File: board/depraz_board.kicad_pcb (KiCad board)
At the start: 2 copper layers, 60 x 40 mm, 43 parts, among them J1 Switches, J2 Host, J3 SWD, J4 SERIAL, U1 TLV75519PDRV, U2 TLV75533PDRV, U5 PMW3389DM, U6 STM32F103C8Tx, Y1 8MHz

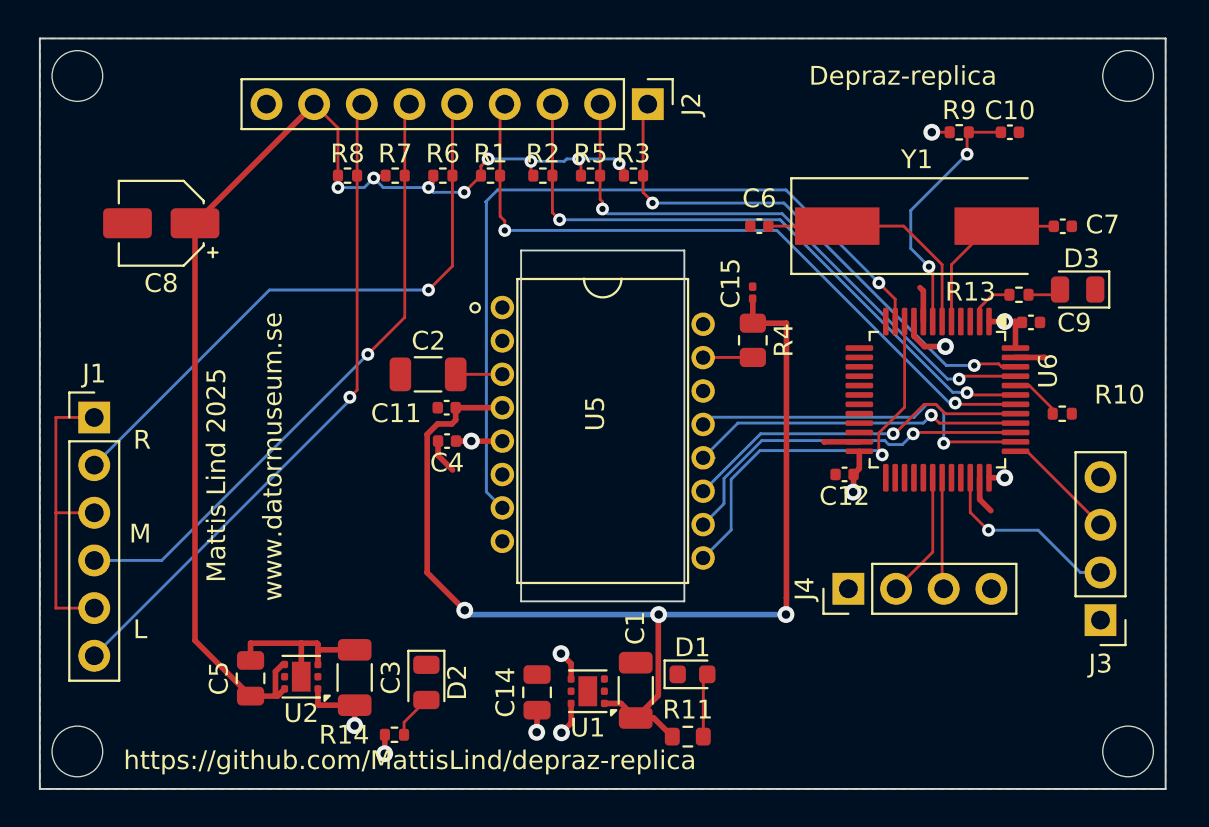
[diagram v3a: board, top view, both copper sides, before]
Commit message: Fixed layout after review.
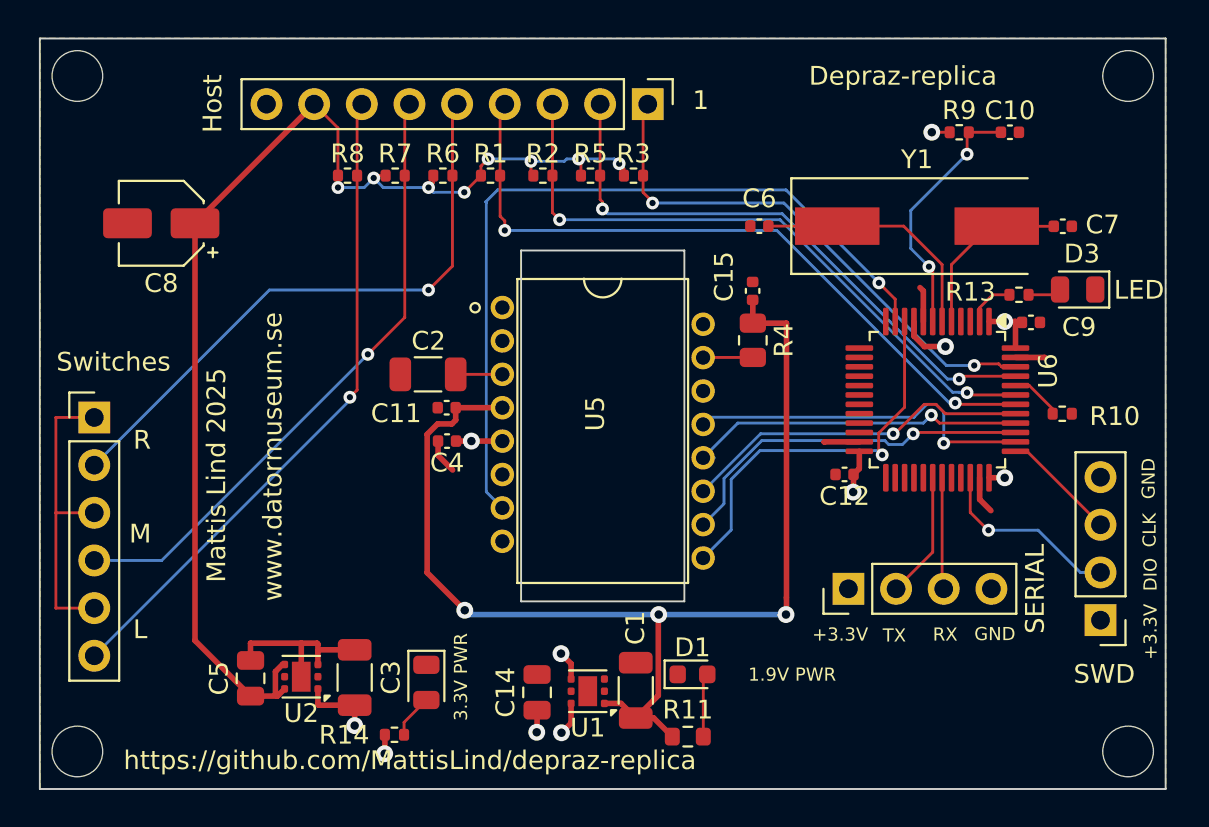
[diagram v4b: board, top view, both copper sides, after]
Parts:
- C15: footprint Capacitor_SMD:C_0201_0603Metric -> Capacitor_SMD:C_0402_1005Metric
- moved C15 0.09 mm to (158.0, 73.5)
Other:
- board text added: "+3.3V"
- board text added: "1"
- board text added: "CLK"
- board text added: "DIO"
- board text added: "GND"
- board text added: "RX"
- board text added: "TX"
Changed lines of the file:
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@@
 			(at 0 -2.33 0)
 			(layer "F.SilkS")
+			(hide yes)
 			(effects
 				(font
@@
 		)
 		(property "Value" "Switches"
-			(at 0 15.03 0)
-			(layer "F.Fab")
+			(at 1.0266 -2.9586 0)
+			(layer "F.SilkS")
 			(effects
 				(font
@@
 			(at 0 -2.33 0)
 			(layer "F.SilkS")
+			(hide yes)
 			(effects
 				(font
@@
 		)
 		(property "Value" "SWD"
-			(at 0 9.95 0)
-			(layer "F.Fab")
+			(at -0.2032 -2.8784 0)
+			(layer "F.SilkS")
 			(effects
 				(font
@@
 			(at 0 -2.33 90)
 			(layer "F.SilkS")
+			(hide yes)
 			(effects
 				(font
@@
 		)
 		(property "Value" "Host"
-			(at 0 22.65 90)
-			(layer "F.Fab")
+			(at -0.0254 23.1902 90)
+			(layer "F.SilkS")
 			(effects
 				(font
@@
 			(at 0 -2.33 90)
 			(layer "F.SilkS")
+			(hide yes)
 			(effects
 				(font
@@
 		(property "Value" "SERIAL"
 			(at 0 9.95 90)
-			(layer "F.Fab")
+			(layer "F.SilkS")
 			(effects
 				(font
@@
 		(tags "resistor")
 		(property "Reference" "R10"
-			(at 3.056 -1.006 0)
+			(at 2.802 0.137 0)
 			(layer "F.SilkS")
 			(effects
@@
 		(tags "LED")
 		(property "Reference" "D3"
-			(at -0.2032 1.651 360)
+			(at -0.2286 1.905 360)
 			(layer "F.SilkS")
 			(effects
@@
 		)
 		(property "Value" "LED"
-			(at 0 1.65 360)
-			(layer "F.Fab")
+			(at -3.2766 -0.0254 0)
+			(layer "F.SilkS")
 			(effects
 				(font
@@
 		)
 		(property "Value" "1.9V PWR"
-			(at 0 1.43 0)
-			(layer "F.Fab")
+			(at 5.3137 0.0138 0)
+			(layer "F.SilkS")
 			(effects
 				(font
-					(size 1 1)
-					(thickness 0.15)
+					(size 0.7 0.7)
+					(thickness 0.1)
 				)
 			)
@@
 		(tags "LED")
 		(property "Reference" "D2"
-			(at 0 -1.65 90)
+			(at 2.4794 -0.1668 90)
 			(layer "F.SilkS")
+			(hide yes)
 			(effects
 				(font
@@
 		)
 		(property "Value" "3.3V PWR"
-			(at 0 1.65 90)
-			(layer "F.Fab")
+			(at -0.2892 -1.8432 90)
+			(layer "F.SilkS")
 			(effects
 				(font
-					(size 1 1)
-					(thickness 0.15)
+					(size 0.7 0.7)
+					(thickness 0.1)
 				)
 			)
@@
 		)
 	)
-	(footprint "Capacitor_SMD:C_0201_0603Metric"
+	(footprint "Capacitor_SMD:C_0402_1005Metric"
 		(layer "F.Cu")
-		(at 157.988 73.5482 90)
-		(descr "Capacitor SMD 0201 (0603 Metric), square (rectangular) end terminal, IPC_7351 nominal, (Body size source: https://www.vishay.com/docs/20052/crcw0201e3.pdf), generated with kicad-footprint-generator")
+		(at 157.988 73.4542 90)
+		(descr "Capacitor SMD 0402 (1005 Metric), square (rectangular) end terminal, IPC_7351 nominal, (Body size source: IPC-SM-782 page 76, https://www.pcb-3d.com/wordpress/wp-content/uploads/ipc-sm-782a_amendment_1_and_2.pdf), generated with kicad-footprint-generator")
 		(tags "capacitor")
 		(property "Reference" "C15"
-			(at 0.4978 -1.1684 90)
+			(at 0.7594 -1.524 90)
 			(layer "F.SilkS")
 			(effects
@@
 		)
 		(property "Value" "100n"
-			(at 0 1.05 90)
+			(at 0 1.16 90)
 			(layer "F.Fab")
 			(effects
@@
 			)
 		)
-		(property "Footprint" "Capacitor_SMD:C_0201_0603Metric"
+		(property "Footprint" "Capacitor_SMD:C_0402_1005Metric"
 			(at 0 0 90)
 			(unlocked yes)
@@
 		(attr smd)
 		(fp_line
-			(start 0.7 -0.35)
-			(end 0.7 0.35)
+			(start -0.107836 -0.36)
+			(end 0.107836 -0.36)
+			(stroke
+				(width 0.12)
+				(type solid)
+			)
+			(layer "F.SilkS")
+		)
+		(fp_line
+			(start -0.107836 0.36)
+			(end 0.107836 0.36)
+			(stroke
+				(width 0.12)
+				(type solid)
+			)
+			(layer "F.SilkS")
+		)
+		(fp_line
+			(start 0.91 -0.46)
+			(end 0.91 0.46)
 			(stroke
 				(width 0.05)
@@
 		)
 		(fp_line
-			(start -0.7 -0.35)
-			(end 0.7 -0.35)
+			(start -0.91 -0.46)
+			(end 0.91 -0.46)
 			(stroke
 				(width 0.05)
@@
 		)
 		(fp_line
-			(start 0.7 0.35)
-			(end -0.7 0.35)
+			(start 0.91 0.46)
+			(end -0.91 0.46)
 			(stroke
 				(width 0.05)
@@
 		)
 		(fp_line
-			(start -0.7 0.35)
-			(end -0.7 -0.35)
+			(start -0.91 0.46)
+			(end -0.91 -0.46)
 			(stroke
 				(width 0.05)
@@
 		)
 		(fp_line
-			(start 0.3 -0.15)
-			(end 0.3 0.15)
+			(start 0.5 -0.25)
+			(end 0.5 0.25)
 			(stroke
 				(width 0.1)
@@
 		)
 		(fp_line
-			(start -0.3 -0.15)
-			(end 0.3 -0.15)
+			(start -0.5 -0.25)
+			(end 0.5 -0.25)
 			(stroke
 				(width 0.1)
@@
 		)
 		(fp_line
-			(start 0.3 0.15)
-			(end -0.3 0.15)
+			(start 0.5 0.25)
+			(end -0.5 0.25)
 			(stroke
 				(width 0.1)
@@
 		)
 		(fp_line
-			(start -0.3 0.15)
-			(end -0.3 -0.15)
+			(start -0.5 0.25)
+			(end -0.5 -0.25)
 			(stroke
 				(width 0.1)
@@
 		)
 		(fp_text user "${REFERENCE}"
-			(at 0 -0.68 90)
+			(at 0 0 90)
 			(layer "F.Fab")
 			(effects
@@
 			)
 		)
-		(pad "" smd roundrect
-			(at -0.345 0 90)
-			(size 0.318 0.36)
-			(layers "F.Paste")
-			(roundrect_rratio 0.25)
-		)
-		(pad "" smd roundrect
-			(at 0.345 0 90)
-			(size 0.318 0.36)
-			(layers "F.Paste")
-			(roundrect_rratio 0.25)
-		)
 		(pad "1" smd roundrect
-			(at -0.32 0 90)
-			(size 0.46 0.4)
-			(layers "F.Cu" "F.Mask")
+			(at -0.48 0 90)
+			(size 0.56 0.62)
+			(layers "F.Cu" "F.Paste" "F.Mask")
 			(roundrect_rratio 0.25)
 			(net 53 "+1.9V")
@@
 		)
 		(pad "2" smd roundrect
-			(at 0.32 0 90)
-			(size 0.46 0.4)
-			(layers "F.Cu" "F.Mask")
+			(at 0.48 0 90)
+			(size 0.56 0.62)
+			(layers "F.Cu" "F.Paste" "F.Mask")
 			(roundrect_rratio 0.25)
 			(net 1 "GND")
 			(pintype "passive")
 		)
-		(model "${KICAD8_3DMODEL_DIR}/Capacitor_SMD.3dshapes/C_0201_0603Metric.wrl"
+		(model "${KICAD8_3DMODEL_DIR}/Capacitor_SMD.3dshapes/C_0402_1005Metric.wrl"
 			(offset
 				(xyz 0 0 0)
@@
 		(tags "capacitor")
 		(property "Reference" "C9"
-			(at 2.3088 0.0254 0)
+			(at 2.5628 0.254 0)
 			(layer "F.SilkS")
 			(effects
@@
 		(layer "Edge.Cuts")
 	)
+	(gr_text "CLK"
+		(at 179.5526 87.122 90)
+		(layer "F.SilkS")
+		(effects
+			(font
+				(size 0.7 0.7)
+				(thickness 0.1)
+			)
+			(justify left bottom)
+		)
+	)
 	(gr_text "M"
 		(at 125.35 86.4 0)
@@
 		)
 	)
+	(gr_text "RX"
+		(at 167.5892 92.1766 0)
+		(layer "F.SilkS")
+		(effects
+			(font
+				(size 0.7 0.7)
+				(thickness 0.1)
+			)
+			(justify left bottom)
+		)
+	)
 	(gr_text "R"
 		(at 125.45 81.4 0)
@@
 		)
 	)
+	(gr_text "GND"
+		(at 179.5018 84.5566 90)
+		(layer "F.SilkS")
+		(effects
+			(font
+				(size 0.7 0.7)
+				(thickness 0.1)
+			)
+			(justify left bottom)
+		)
+	)
+	(gr_text "+3.3V"
+		(at 161.163 92.1766 0)
+		(layer "F.SilkS")
+		(effects
+			(font
+				(size 0.7 0.7)
+				(thickness 0.1)
+			)
+			(justify left bottom)
+		)
+	)
 	(gr_text "Depraz-replica"
 		(at 166 62 0)
@@
 		)
 	)
+	(gr_text "DIO"
+		(at 179.6034 89.4588 90)
+		(layer "F.SilkS")
+		(effects
+			(font
+				(size 0.7 0.7)
+				(thickness 0.1)
+			)
+			(justify left bottom)
+		)
+	)
 	(gr_text "www.datormuseum.se"
 		(at 133 90 90)
@@
 		)
 	)
+	(gr_text "TX"
+		(at 164.9222 92.2274 0)
+		(layer "F.SilkS")
+		(effects
+			(font
+				(size 0.7 0.7)
+				(thickness 0.1)
+			)
+			(justify left bottom)
+		)
+	)
+	(gr_text "+3.3V"
+		(at 179.6034 93.1164 90)
+		(layer "F.SilkS")
+		(effects
+			(font
+				(size 0.7 0.7)
+				(thickness 0.1)
+			)
+			(justify left bottom)
+		)
+	)
 	(gr_text "Mattis Lind 2025"
 		(at 130 89 90)
 		(layer "F.SilkS")
 		(effects
+			(font
+				(size 1 1)
+				(thickness 0.15)
+			)
+			(justify left bottom)
+		)
+	)
+	(gr_text "GND"
+		(at 169.799 92.1512 0)
+		(layer "F.SilkS")
+		(effects
+			(font
+				(size 0.7 0.7)
+				(thickness 0.1)
+			)
+			(justify left bottom)
+		)
+	)
+	(gr_text "1"
+		(at 154.7876 63.881 0)
+		(layer "F.SilkS")
+		(effects
